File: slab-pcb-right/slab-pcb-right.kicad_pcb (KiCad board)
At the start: 2 copper layers, 158 x 104 mm, 127 parts, among them J1 MagnetR, J2 MagnetL, J3 TRRS_R, J4 TRRS_L, J5 SSD1306, J6 Conn_01x06, Q1 MMBT3906, SW1 RotaryEncoder, U1 Seeeduino Xiao rp2040, U2 PCA9555PW, U3 PCA9555PW, U4 ADS1110, U5 PW14

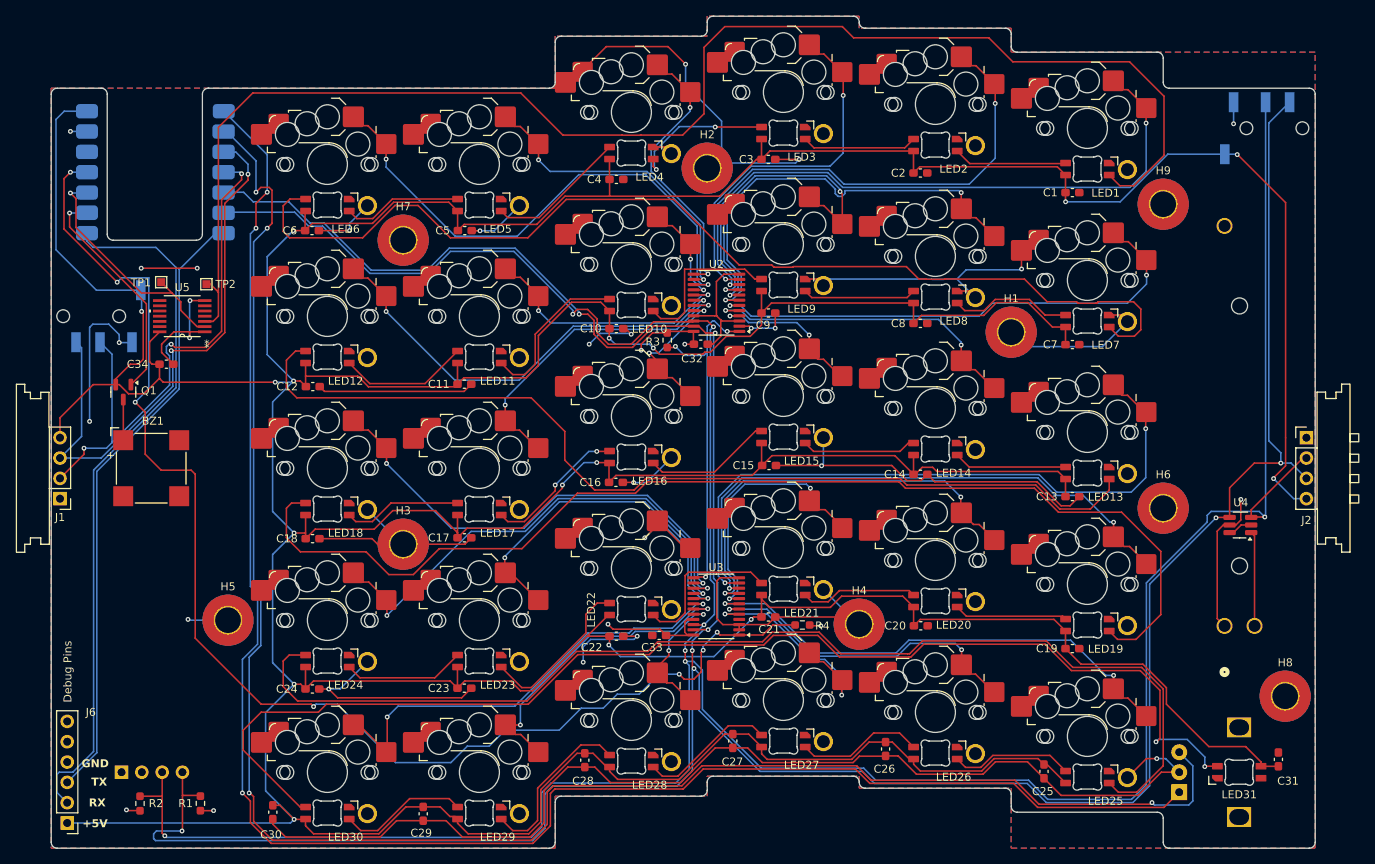
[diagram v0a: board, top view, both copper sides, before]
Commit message: fix: upside-down magnetic connectors
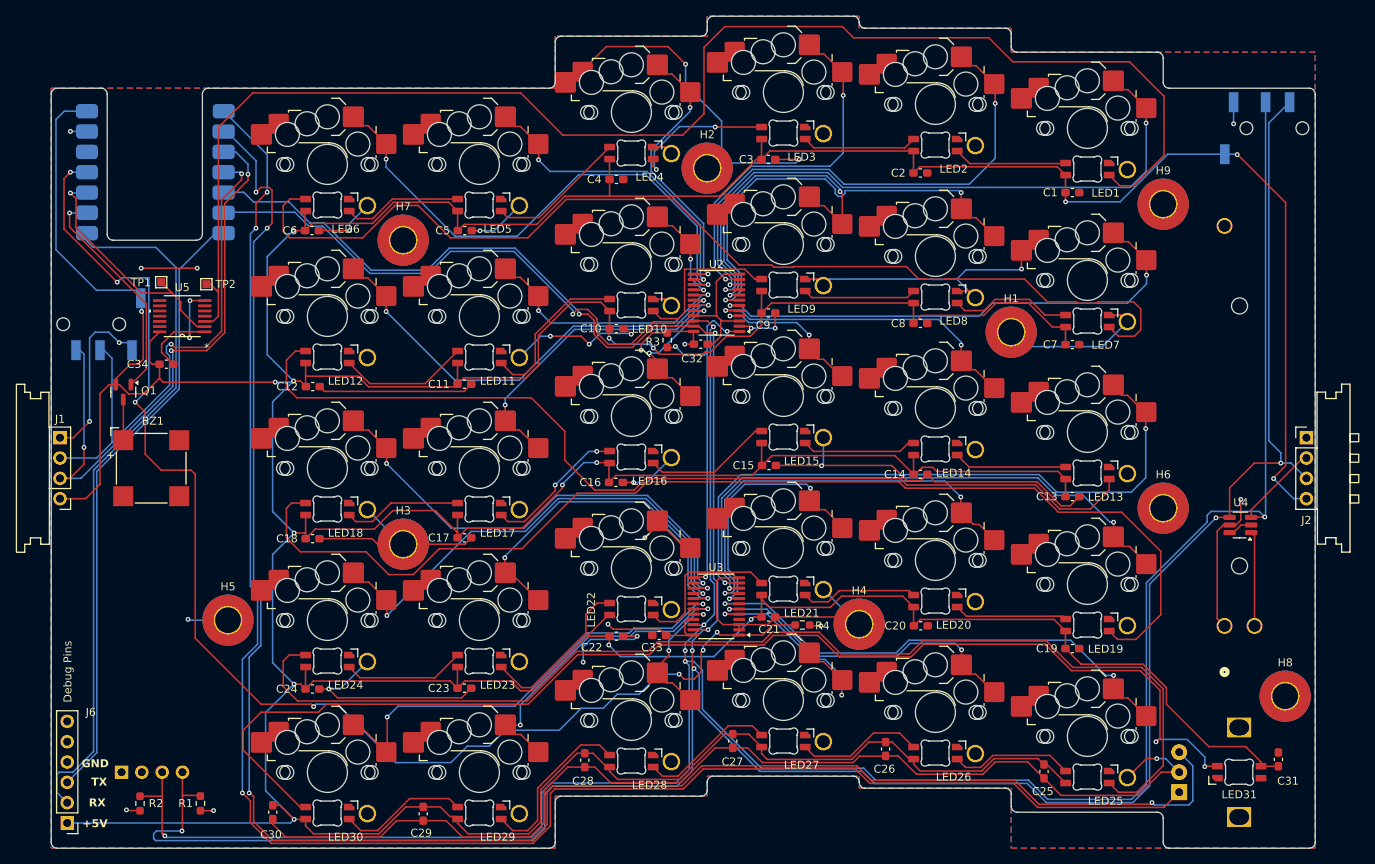
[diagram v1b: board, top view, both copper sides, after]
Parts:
- moved J3 1.00 mm to (76.2, 84.5)
- turned J1 to 0 degrees
- renumbered REF** to OSHW, REF** to WEEE
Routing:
- net GND: track 506.5 -> 522.0 mm, vias 22 -> 23
- net VBUS: track 927.5 -> 935.8 mm
- net /I2C0_SDA: track 72.9 -> 76.9 mm, vias 2 -> 3
- net /I2C0_SCL: track 69.2 -> 67.2 mm, vias 3 -> 2

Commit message: fix: add voltage divider to potentiometer
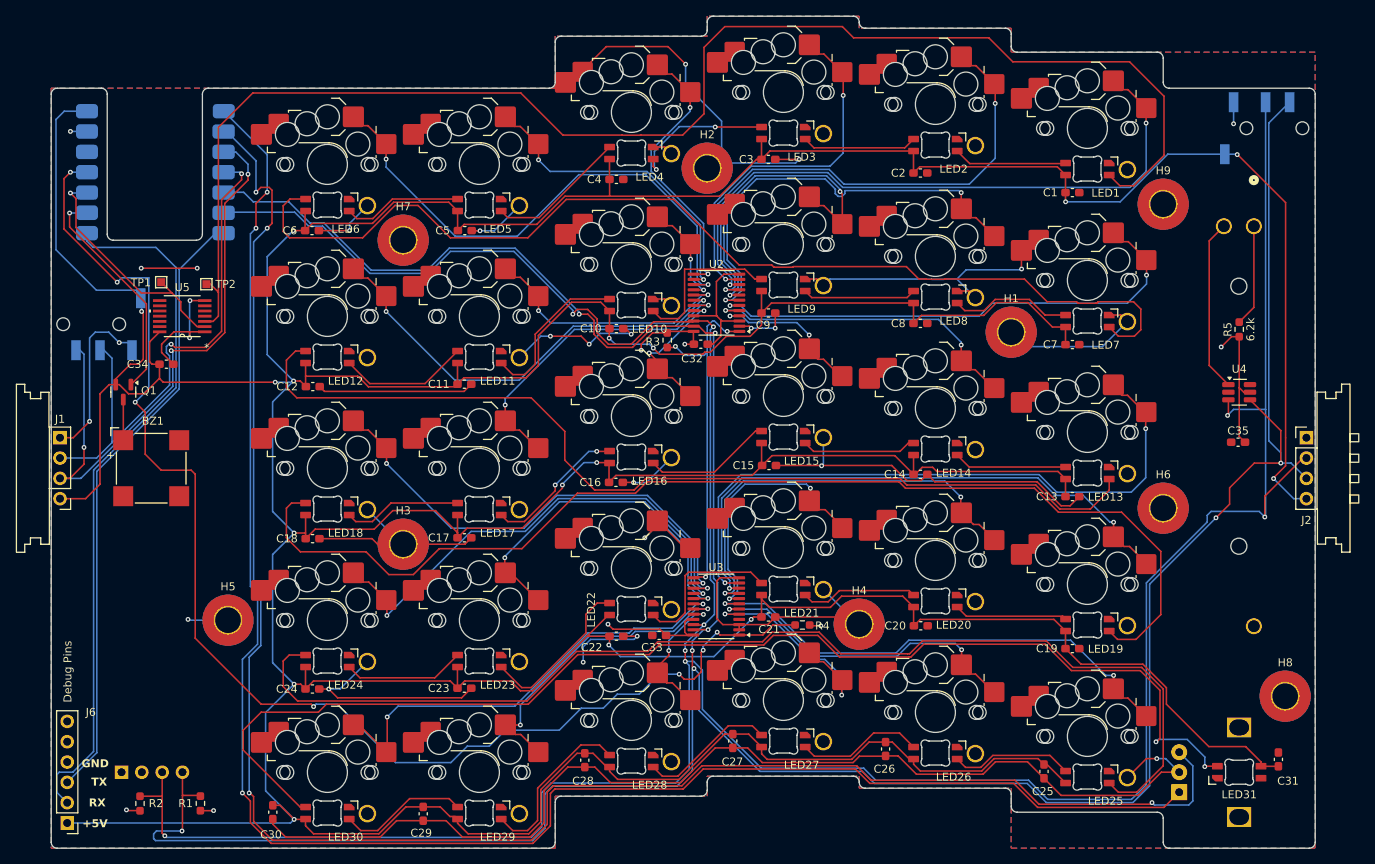
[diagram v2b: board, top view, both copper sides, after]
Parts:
- added C35: 100nF, Capacitor_SMD:C_0603_1608Metric_Pad1.08x0.95mm_HandSolder, F.Cu at (218.4, 99.2)
- added R5: 6.2k, Resistor_SMD:R_0603_1608Metric_Pad0.98x0.95mm_HandSolder, F.Cu at (218.5, 85.2)
- U5: value PW14 -> SN74AHCT125PWR
- moved RV1 50.1 mm to (220.3, 72.2), turned to -90 degrees
- moved U4 16.6 mm to (218.5, 93.0), turned to 0 degrees
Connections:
- RV1 pad 1: +3V3 -> Net-(R5-Pad2)
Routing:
- net Net-(R5-Pad2): track 0.00 -> 12.7 mm
- net Net-(U4-VIN+): track 11.8 -> 21.6 mm
- net /I2C1_SDA: track 390.0 -> 398.5 mm
- net /I2C1_SCL: track 393.2 -> 397.8 mm, vias 7 -> 8
- net GND: track 522.0 -> 518.9 mm
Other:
- board text added: "version 3.1 'nowhere'"
- board text removed: "version 3.0 'nowhere'"

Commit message: feat: use slots instead of overlapped drill hits
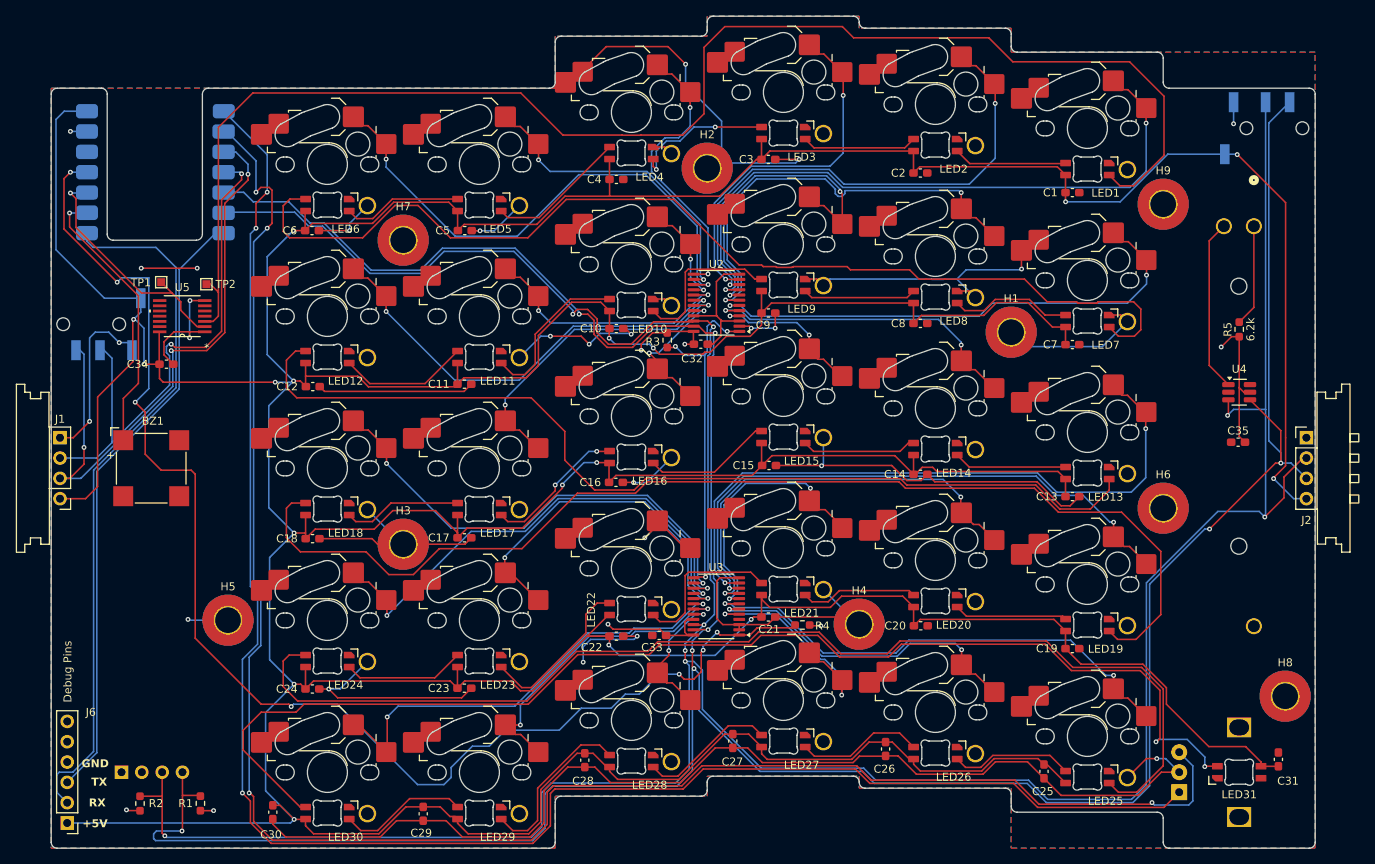
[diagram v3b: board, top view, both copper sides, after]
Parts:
- removed Q1: MMBT3906, Package_TO_SOT_SMD:SOT-23
- BZ1: footprint Buzzer_Beeper:MagneticBuzzer_CUI_CMT-8504-100-SMT -> CustomFootprints:buzzer
- U5: value SN74AHCT125PWR -> (none)
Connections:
- BZ1 pad 1: Net-(BZ1-+) -> /BUZZER
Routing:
- net /BUZZER: track 27.4 -> 33.9 mm
- net Net-(BZ1-+): track 5.08 -> 0.00 mm
- net /EXPANDER2_INT: track 164.6 -> 167.6 mm
- net VBUS: track 935.8 -> 934.4 mm, vias 16 -> 17
- net /KEY4: track 35.2 -> 36.1 mm
- net /I2C1_SDA: track 398.5 -> 397.6 mm
- net /KEY19: track 72.5 -> 73.1 mm
- net /KEY13: track 82.4 -> 83.0 mm
- net /KEY20: track 53.4 -> 54.0 mm

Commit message: feat: bump to 3.2
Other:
- board text added: "version 3.2 'nowhere'"
- board text removed: "version 3.1 'nowhere'"
